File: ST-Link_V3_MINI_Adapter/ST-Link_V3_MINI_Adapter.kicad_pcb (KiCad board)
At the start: 2 copper layers, 20.3 x 20 mm, 8 parts, among them J1 Conn_02x07_Odd_Even, J2 Conn_02x10_Odd_Even, J4 Conn_01x04, J5 Conn_01x06, SW1 SW_Push

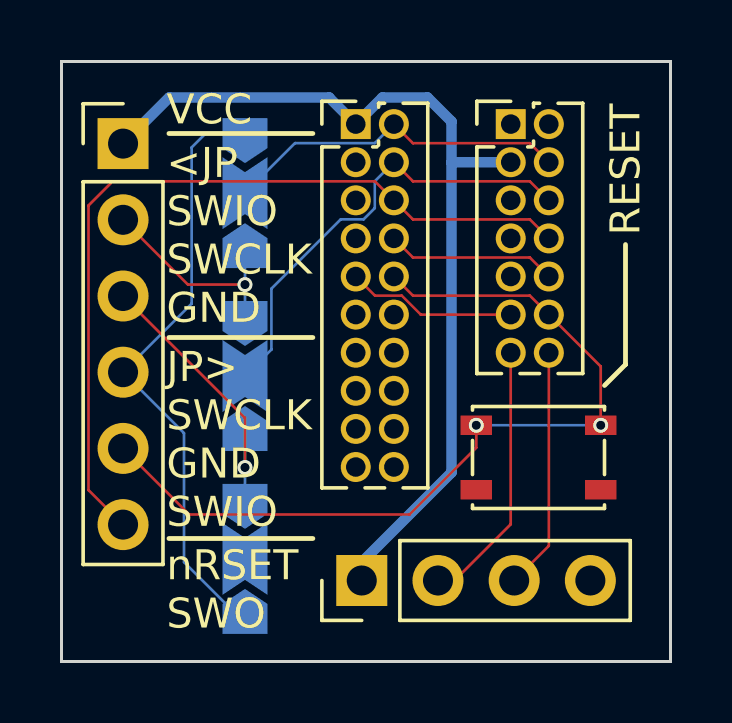
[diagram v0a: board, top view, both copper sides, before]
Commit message: [ST-Link_V3_MINI_Adapter] Minor pcb size and copper fill adjust
Signed-off-by: Adam BZH <424778940z@users.noreply.github.com>
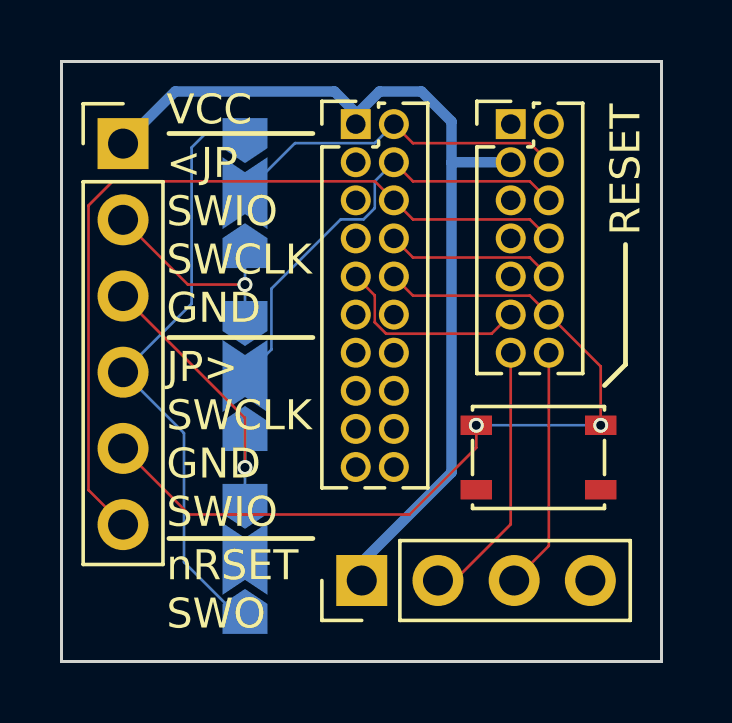
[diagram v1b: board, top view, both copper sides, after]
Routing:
- net /GND_DETECT: track 5.69 -> 6.99 mm
- net /VCC: track 31.2 -> 31.9 mm
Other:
- board size 20.3 x 20 mm -> 20 x 20 mm
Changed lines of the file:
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@@
   (gr_line (start 125.48 48.5) (end 130.28 48.5) (layer "F.SilkS") (width 0.16))
   (gr_line (start 140.7 49.4) (end 140 50.1) (layer "F.SilkS") (width 0.16))
-  (gr_line (start 142.2 59.3) (end 121.9 59.3) (layer "Edge.Cuts") (width 0.1))
+  (gr_line (start 141.9 59.3) (end 121.9 59.3) (layer "Edge.Cuts") (width 0.1))
   (gr_line (start 121.9 59.3) (end 121.9 39.3) (layer "Edge.Cuts") (width 0.1))
-  (gr_line (start 142.2 39.3) (end 142.2 59.3) (layer "Edge.Cuts") (width 0.1))
-  (gr_line (start 121.9 39.3) (end 142.2 39.3) (layer "Edge.Cuts") (width 0.1))
+  (gr_line (start 141.9 39.3) (end 141.9 59.3) (layer "Edge.Cuts") (width 0.1))
+  (gr_line (start 121.9 39.3) (end 141.9 39.3) (layer "Edge.Cuts") (width 0.1))
   (gr_text "STDC14" (at 140.2 43.7 90) (layer "B.SilkS")
     (effects (font (size 1 1) (thickness 0.15)) (justify mirror))
@@
   (segment (start 133.615989 45.833989) (end 132.979 45.197) (width 0.089) (layer "F.Cu") (net 7))
   (segment (start 138.1445 46.467) (end 137.511489 45.833989) (width 0.089) (layer "F.Cu") (net 7))
-  (segment (start 132.345989 47.103989) (end 131.709 46.467) (width 0.089) (layer "F.Cu") (net 8))
-  (segment (start 133.874214 47.737) (end 133.241203 47.103989) (width 0.089) (layer "F.Cu") (net 8))
-  (segment (start 133.241203 47.103989) (end 132.345989 47.103989) (width 0.089) (layer "F.Cu") (net 8))
-  (segment (start 136.8745 47.737) (end 133.874214 47.737) (width 0.089) (layer "F.Cu") (net 8))
-  (segment (start 132.596 40.5) (end 131.709 41.387) (width 0.35) (layer "B.Cu") (net 9))
+  (segment (start 136.237511 48.373989) (end 132.720775 48.373989) (width 0.089) (layer "F.Cu") (net 8))
+  (segment (start 136.8745 47.737) (end 136.237511 48.373989) (width 0.089) (layer "F.Cu") (net 8))
+  (segment (start 132.342011 47.100011) (end 131.709 46.467) (width 0.089) (layer "F.Cu") (net 8))
+  (segment (start 131.709 46.709) (end 131.709 46.467) (width 0.089) (layer "F.Cu") (net 8))
+  (segment (start 132.720775 48.373989) (end 132.342011 47.995225) (width 0.089) (layer "F.Cu") (net 8))
+  (segment (start 132.342011 47.995225) (end 132.342011 47.100011) (width 0.089) (layer "F.Cu") (net 8))
+  (segment (start 125.689 40.3) (end 131 40.3) (width 0.35) (layer "B.Cu") (net 9))
+  (segment (start 131.709 41.091) (end 131.709 41.387) (width 0.35) (layer "B.Cu") (net 9))
   (segment (start 136.8745 42.657) (end 134.9 42.657) (width 0.35) (layer "B.Cu") (net 9))
+  (segment (start 123.952 42.037) (end 125.689 40.3) (width 0.35) (layer "B.Cu") (net 9))
+  (segment (start 131 40.3) (end 131.709 41.009) (width 0.35) (layer "B.Cu") (net 9))
+  (segment (start 134.9 41.3) (end 133.9 40.3) (width 0.35) (layer "B.Cu") (net 9))
   (segment (start 134.9 42.657) (end 134.9 53) (width 0.35) (layer "B.Cu") (net 9))
   (segment (start 131.909 55.991) (end 131.909 56.6) (width 0.35) (layer "B.Cu") (net 9))
-  (segment (start 125.489 40.5) (end 130.822 40.5) (width 0.35) (layer "B.Cu") (net 9))
   (segment (start 134.9 53) (end 131.909 55.991) (width 0.35) (layer "B.Cu") (net 9))
-  (segment (start 123.952 42.037) (end 125.489 40.5) (width 0.35) (layer "B.Cu") (net 9))
-  (segment (start 130.822 40.5) (end 131.709 41.387) (width 0.35) (layer "B.Cu") (net 9))
-  (segment (start 134.9 41.3) (end 134.1 40.5) (width 0.35) (layer "B.Cu") (net 9))
-  (segment (start 134.1 40.5) (end 132.596 40.5) (width 0.35) (layer "B.Cu") (net 9))
-  (segment (start 134.9 41.3) (end 134.9 42.657) (width 0.35) (layer "B.Cu") (net 9))
+  (segment (start 131.709 41.009) (end 131.709 41.387) (width 0.35) (layer "B.Cu") (net 9))
+  (segment (start 134.9 42.657) (end 134.9 41.3) (width 0.35) (layer "B.Cu") (net 9))
+  (segment (start 133.9 40.3) (end 132.5 40.3) (width 0.35) (layer "B.Cu") (net 9))
+  (segment (start 132.5 40.3) (end 131.709 41.091) (width 0.35) (layer "B.Cu") (net 9))
   (segment (start 136.8745 54.7255) (end 136.8745 49.007) (width 0.089) (layer "F.Cu") (net 10))
   (segment (start 135 56.6) (end 136.8745 54.7255) (width 0.089) (layer "F.Cu") (net 10))
@@
   (segment (start 135.725 51.425) (end 139.875 51.425) (width 0.089) (layer "B.Cu") (net 22))
   (zone (net 4) (net_name "/GND") (layers F&B.Cu) (hatch edge 0.508)
-    (connect_pads (clearance 0.508))
-    (min_thickness 0.254) (filled_areas_thickness no)
+    (connect_pads yes (clearance 0.089))
+    (min_thickness 0.089) (filled_areas_thickness no)
     (fill yes (thermal_gap 0.508) (thermal_bridge_width 0.508))
     (polygon
       (pts
-        (xy 142.2 59.3)
+        (xy 141.9 59.3)
         (xy 121.9 59.3)
         (xy 121.9 39.3)
-        (xy 142.2 39.3)
+        (xy 141.9 39.3)
       )
     )
